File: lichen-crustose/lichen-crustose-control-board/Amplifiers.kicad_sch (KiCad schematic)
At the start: 21 parts

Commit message: Updates Lichen symbols and footprints. Fixes to Crustose and Vactrol VCA. Adds 3D model of the RP2350 dual USB board.
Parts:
- R10, R13, R14: value 4.7k_0603 -> 5.1k_0603; JLCPCB ID C23162 -> (none); Specifications 4k7, 1%, 1/10W, 0603 -> 5.1K, 1%, 1/10W, 0603
- R11, R12, R35, R36, R37, R38, R39, R40: value 100k_0603 -> 10k_0603
- R9: JLCPCB ID C23186 -> (none)
- RV1, RV2: symbol Lichen:Potentiometer -> Lichen:R_Potentiometer; now left out of the parts list
- RV10, RV3, RV4: symbol Device:R_Potentiometer_Dual -> Lichen:R_Potentiometer_Dual; now left out of the parts list
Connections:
- net CARRER_AMPLIFICATION_R: now also RV4.2; no longer RV4.5
- net CARRIER_AMPLIFICATION_L: now also RV4.5; no longer RV4.2
- net CARRIER_L: now also RV4.6; no longer RV4.1
- net CARRIER_R: now also RV4.3; no longer RV4.4
- net CARRIER_UNAMPLIFIED_L: now also RV4.1, RV4.4; no longer RV4.3, RV4.6
- net FB_L: now also RV10.6; no longer RV10.1
- net FB_R: now also RV10.3; no longer RV10.4
- net FEEDBACK_MIX_L: now also RV10.5; no longer RV10.2
- net FEEDBACK_MIX_R: now also RV10.2; no longer RV10.5
- net GND: now also RV10.1, RV10.4; no longer RV10.3, RV10.6
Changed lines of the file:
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@@
 			)
 		)
-		(property "JLCPCB ID" " C23186"
-			(at 81.28 71.12 0)
-			(effects
-				(font
-					(size 1.27 1.27)
-				)
-				(hide yes)
-			)
-		)
 		(property "LCSC" "C23186"
 			(at 98.298 74.168 0)
@@
 			)
 		)
-		(property "Value" "100k_0603"
+		(property "Value" "10k_0603"
 			(at 198.12 90.17 90)
 			(effects
@@
 			)
 		)
-		(property "Datasheet" "https://www.lcsc.com/datasheet/lcsc_datasheet_2206010045_UNI-ROYAL-Uniroyal-Elec-0603WAF1003T5E_C25803.pdf"
+		(property "Datasheet" "https://jlcpcb.com/api/file/downloadByFileSystemAccessId/8579706381320323072"
 			(at 198.12 92.71 0)
 			(effects
@@
 	)
 	(symbol
-		(lib_id "Device:R_Potentiometer_Dual")
+		(lib_id "Lichen:R_Potentiometer_Dual")
 		(at 100.33 68.58 0)
 		(unit 1)
 		(exclude_from_sim no)
-		(in_bom yes)
+		(in_bom no)
 		(on_board yes)
 		(dnp no)
@@
 		)
 		(property "Footprint" "Lichen:Potentiometer_Alpha_RD902F-40-00D_Dual_Vertical"
-			(at 106.68 70.485 0)
+			(at 107.188 80.518 0)
 			(effects
 				(font
@@
 		)
 		(property "Datasheet" "https://www.thonk.co.uk/shop/alpha-9mm-pots-vert-t18-dual-gang/"
-			(at 106.68 70.485 0)
+			(at 106.934 77.724 0)
 			(effects
 				(font
@@
 		)
 		(property "Description" "Dual potentiometer"
-			(at 100.33 68.58 0)
+			(at 100.076 83.312 0)
 			(effects
 				(font
@@
 		)
 		(property "Manufacturer" "Alpha"
-			(at 100.33 68.58 90)
+			(at 100.33 85.852 0)
 			(effects
 				(font
@@
 		)
 		(property "Part Number" "RD90F-40"
-			(at 100.33 68.58 90)
+			(at 100.33 88.138 0)
 			(effects
 				(font
@@
 			)
 		)
-		(property "Value" "4.7k_0603"
+		(property "Value" "5.1k_0603"
 			(at 83.82 129.54 90)
 			(effects
@@
 			)
 		)
-		(property "Specifications" "4k7, 1%, 1/10W, 0603"
+		(property "Specifications" "5.1K, 1%, 1/10W, 0603"
 			(at 91.694 129.54 0)
 			(effects
@@
 			)
 		)
-		(property "JLCPCB ID" "C23162"
-			(at 83.82 132.08 0)
-			(effects
-				(font
-					(size 1.27 1.27)
-				)
-				(hide yes)
-			)
-		)
 		(property "LCSC" "C23186"
 			(at 100.838 135.128 0)
@@
 	)
 	(symbol
-		(lib_id "Lichen:Potentiometer")
+		(lib_id "Lichen:R_Potentiometer")
 		(at 71.12 149.86 0)
 		(mirror x)
 		(unit 1)
 		(exclude_from_sim no)
-		(in_bom yes)
+		(in_bom no)
 		(on_board yes)
 		(dnp no)
 		(fields_autoplaced yes)
 		(property "Reference" "RV1"
-			(at 68.58 151.1301 0)
+			(at 67.31 148.5899 0)
 			(effects
 				(font
@@
 		)
 		(property "Value" "B10K"
-			(at 68.58 148.5901 0)
+			(at 67.31 151.1299 0)
 			(effects
 				(font
@@
 			)
 		)
-		(property "Value" "100k_0603"
+		(property "Value" "10k_0603"
 			(at 198.12 72.39 90)
 			(effects
@@
 			)
 		)
-		(property "Datasheet" "https://www.lcsc.com/datasheet/lcsc_datasheet_2206010045_UNI-ROYAL-Uniroyal-Elec-0603WAF1003T5E_C25803.pdf"
+		(property "Datasheet" "https://jlcpcb.com/api/file/downloadByFileSystemAccessId/8579706381320323072"
 			(at 198.12 74.93 0)
 			(effects
@@
 			)
 		)
-		(property "Value" "100k_0603"
+		(property "Value" "10k_0603"
 			(at 83.82 147.32 90)
 			(effects
@@
 			)
 		)
-		(property "Datasheet" "https://www.lcsc.com/datasheet/lcsc_datasheet_2206010045_UNI-ROYAL-Uniroyal-Elec-0603WAF1003T5E_C25803.pdf"
+		(property "Datasheet" "https://jlcpcb.com/api/file/downloadByFileSystemAccessId/8579706381320323072"
 			(at 83.82 149.86 0)
 			(effects
@@
 			)
 		)
-		(property "Datasheet" ""
+		(property "Datasheet" "https://jlcpcb.com/api/file/downloadByFileSystemAccessId/8579707056569573376"
 			(at 217.17 72.39 0)
 			(effects
@@
 			)
 		)
-		(property "Value" "4.7k_0603"
+		(property "Value" "5.1k_0603"
 			(at 83.82 119.38 90)
 			(effects
@@
 			)
 		)
-		(property "Specifications" "4k7, 1%, 1/10W, 0603"
+		(property "Specifications" "5.1K, 1%, 1/10W, 0603"
 			(at 91.694 119.38 0)
 			(effects
@@
 			)
 		)
-		(property "JLCPCB ID" "C23162"
-			(at 83.82 121.92 0)
-			(effects
-				(font
-					(size 1.27 1.27)
-				)
-				(hide yes)
-			)
-		)
 		(property "LCSC" "C23186"
 			(at 100.838 124.968 0)
@@
 			)
 		)
-		(property "Value" "100k_0603"
+		(property "Value" "10k_0603"
 			(at 198.12 43.18 90)
 			(effects
@@
 			)
 		)
-		(property "Datasheet" "https://www.lcsc.com/datasheet/lcsc_datasheet_2206010045_UNI-ROYAL-Uniroyal-Elec-0603WAF1003T5E_C25803.pdf"
+		(property "Datasheet" "https://jlcpcb.com/api/file/downloadByFileSystemAccessId/8579706381320323072"
 			(at 198.12 45.72 0)
 			(effects
@@
 			)
 		)
-		(property "Value" "100k_0603"
+		(property "Value" "10k_0603"
 			(at 83.82 173.99 90)
 			(effects
@@
 			)
 		)
-		(property "Datasheet" "https://www.lcsc.com/datasheet/lcsc_datasheet_2206010045_UNI-ROYAL-Uniroyal-Elec-0603WAF1003T5E_C25803.pdf"
+		(property "Datasheet" "https://jlcpcb.com/api/file/downloadByFileSystemAccessId/8579706381320323072"
 			(at 83.82 176.53 0)
 			(effects
@@
 			)
 		)
-		(property "Value" "4.7k_0603"
+		(property "Value" "5.1k_0603"
 			(at 81.28 80.01 90)
 			(effects
@@
 			)
 		)
-		(property "Specifications" "4k7, 1%, 1/10W, 0603"
+		(property "Specifications" "5.1K, 1%, 1/10W, 0603"
 			(at 89.154 80.01 0)
 			(effects
@@
 			)
 		)
-		(property "JLCPCB ID" "C23162"
-			(at 81.28 82.55 0)
-			(effects
-				(font
-					(size 1.27 1.27)
-				)
-				(hide yes)
-			)
-		)
 		(property "LCSC" "C23186"
 			(at 98.298 85.598 0)
@@
 			)
 		)
-		(property "Value" "100k_0603"
+		(property "Value" "10k_0603"
 			(at 215.9 39.37 90)
 			(effects
@@
 			)
 		)
-		(property "Datasheet" "https://www.lcsc.com/datasheet/lcsc_datasheet_2206010045_UNI-ROYAL-Uniroyal-Elec-0603WAF1003T5E_C25803.pdf"
+		(property "Datasheet" "https://jlcpcb.com/api/file/downloadByFileSystemAccessId/8579706381320323072"
 			(at 215.9 36.83 0)
 			(effects
@@
 			)
 		)
-		(property "Value" "100k_0603"
+		(property "Value" "10k_0603"
 			(at 217.17 86.36 90)
 			(effects
@@
 			)
 		)
-		(property "Datasheet" "https://www.lcsc.com/datasheet/lcsc_datasheet_2206010045_UNI-ROYAL-Uniroyal-Elec-0603WAF1003T5E_C25803.pdf"
+		(property "Datasheet" "https://jlcpcb.com/api/file/downloadByFileSystemAccessId/8579706381320323072"
 			(at 217.17 83.82 0)
 			(effects
@@
 	)
 	(symbol
-		(lib_id "Device:R_Potentiometer_Dual")
+		(lib_id "Lichen:R_Potentiometer_Dual")
 		(at 189.23 68.58 270)
+		(mirror x)
 		(unit 1)
 		(exclude_from_sim no)
-		(in_bom yes)
+		(in_bom no)
 		(on_board yes)
 		(dnp no)
 		(property "Reference" "RV10"
-			(at 183.134 61.976 0)
+			(at 183.134 75.184 0)
 			(effects
 				(font
@@
 		)
 		(property "Value" "B10k_Dual"
-			(at 183.134 75.438 0)
+			(at 183.134 61.722 0)
 			(effects
 				(font
@@
 		)
 		(property "Footprint" "Lichen:Potentiometer_Alpha_RD902F-40-00D_Dual_Vertical"
-			(at 187.325 74.93 0)
+			(at 177.292 61.722 0)
 			(effects
 				(font
@@
 		)
 		(property "Datasheet" "https://www.thonk.co.uk/shop/alpha-9mm-pots-vert-t18-dual-gang/"
-			(at 187.325 74.93 0)
+			(at 180.086 61.976 0)
 			(effects
 				(font
@@
 		)
 		(property "Description" "Dual potentiometer"
-			(at 189.23 68.58 0)
+			(at 174.498 68.834 0)
 			(effects
 				(font
@@
 		)
 		(property "Manufacturer" "Alpha"
-			(at 189.23 68.58 90)
+			(at 171.958 68.58 0)
 			(effects
 				(font
@@
 		)
 		(property "Part Number" "RD90F-40"
-			(at 189.23 68.58 90)
+			(at 169.672 68.58 0)
 			(effects
 				(font
@@
 	)
 	(symbol
-		(lib_id "Device:R_Potentiometer_Dual")
-		(at 121.92 143.51 180)
+		(lib_id "Lichen:R_Potentiometer_Dual")
+		(at 121.92 143.51 0)
+		(mirror x)
 		(unit 1)
 		(exclude_from_sim no)
-		(in_bom yes)
+		(in_bom no)
 		(on_board yes)
 		(dnp no)
 		(property "Reference" "RV4"
-			(at 128.524 137.414 0)
+			(at 115.316 137.414 0)
 			(effects
 				(font
@@
 		)
 		(property "Value" "A10k_Dual"
-			(at 115.062 137.414 0)
+			(at 128.778 137.414 0)
 			(effects
 				(font
@@
 		)
 		(property "Footprint" "Lichen:Potentiometer_Alpha_RD902F-40-00D_Dual_Vertical"
-			(at 115.57 141.605 0)
+			(at 128.778 131.572 0)
 			(effects
 				(font
@@
 		)
 		(property "Datasheet" "https://www.thonk.co.uk/shop/alpha-9mm-pots-vert-t18-dual-gang/"
-			(at 115.57 141.605 0)
+			(at 128.524 134.366 0)
 			(effects
 				(font
@@
 		)
 		(property "Description" "Dual potentiometer"
-			(at 121.92 143.51 0)
+			(at 121.666 128.778 0)
 			(effects
 				(font
@@
 		)
 		(property "Manufacturer" "Alpha"
-			(at 121.92 143.51 90)
+			(at 121.92 126.238 0)
 			(effects
 				(font
@@
 		)
 		(property "Part Number" "RD90F-40"
-			(at 121.92 143.51 90)
+			(at 121.92 123.952 0)
 			(effects
 				(font
@@
 	)
 	(symbol
-		(lib_id "Lichen:Potentiometer")
+		(lib_id "Lichen:R_Potentiometer")
 		(at 71.12 176.53 0)
 		(mirror x)
 		(unit 1)
 		(exclude_from_sim no)
-		(in_bom yes)
+		(in_bom no)
 		(on_board yes)
 		(dnp no)
@@
 			)
 		)
-		(property "Value" "100k_0603"
+		(property "Value" "10k_0603"
 			(at 198.12 59.69 90)
 			(effects
@@
 			)
 		)
-		(property "Datasheet" "https://www.lcsc.com/datasheet/lcsc_datasheet_2206010045_UNI-ROYAL-Uniroyal-Elec-0603WAF1003T5E_C25803.pdf"
+		(property "Datasheet" "https://jlcpcb.com/api/file/downloadByFileSystemAccessId/8579706381320323072"
 			(at 198.12 62.23 0)
 			(effects

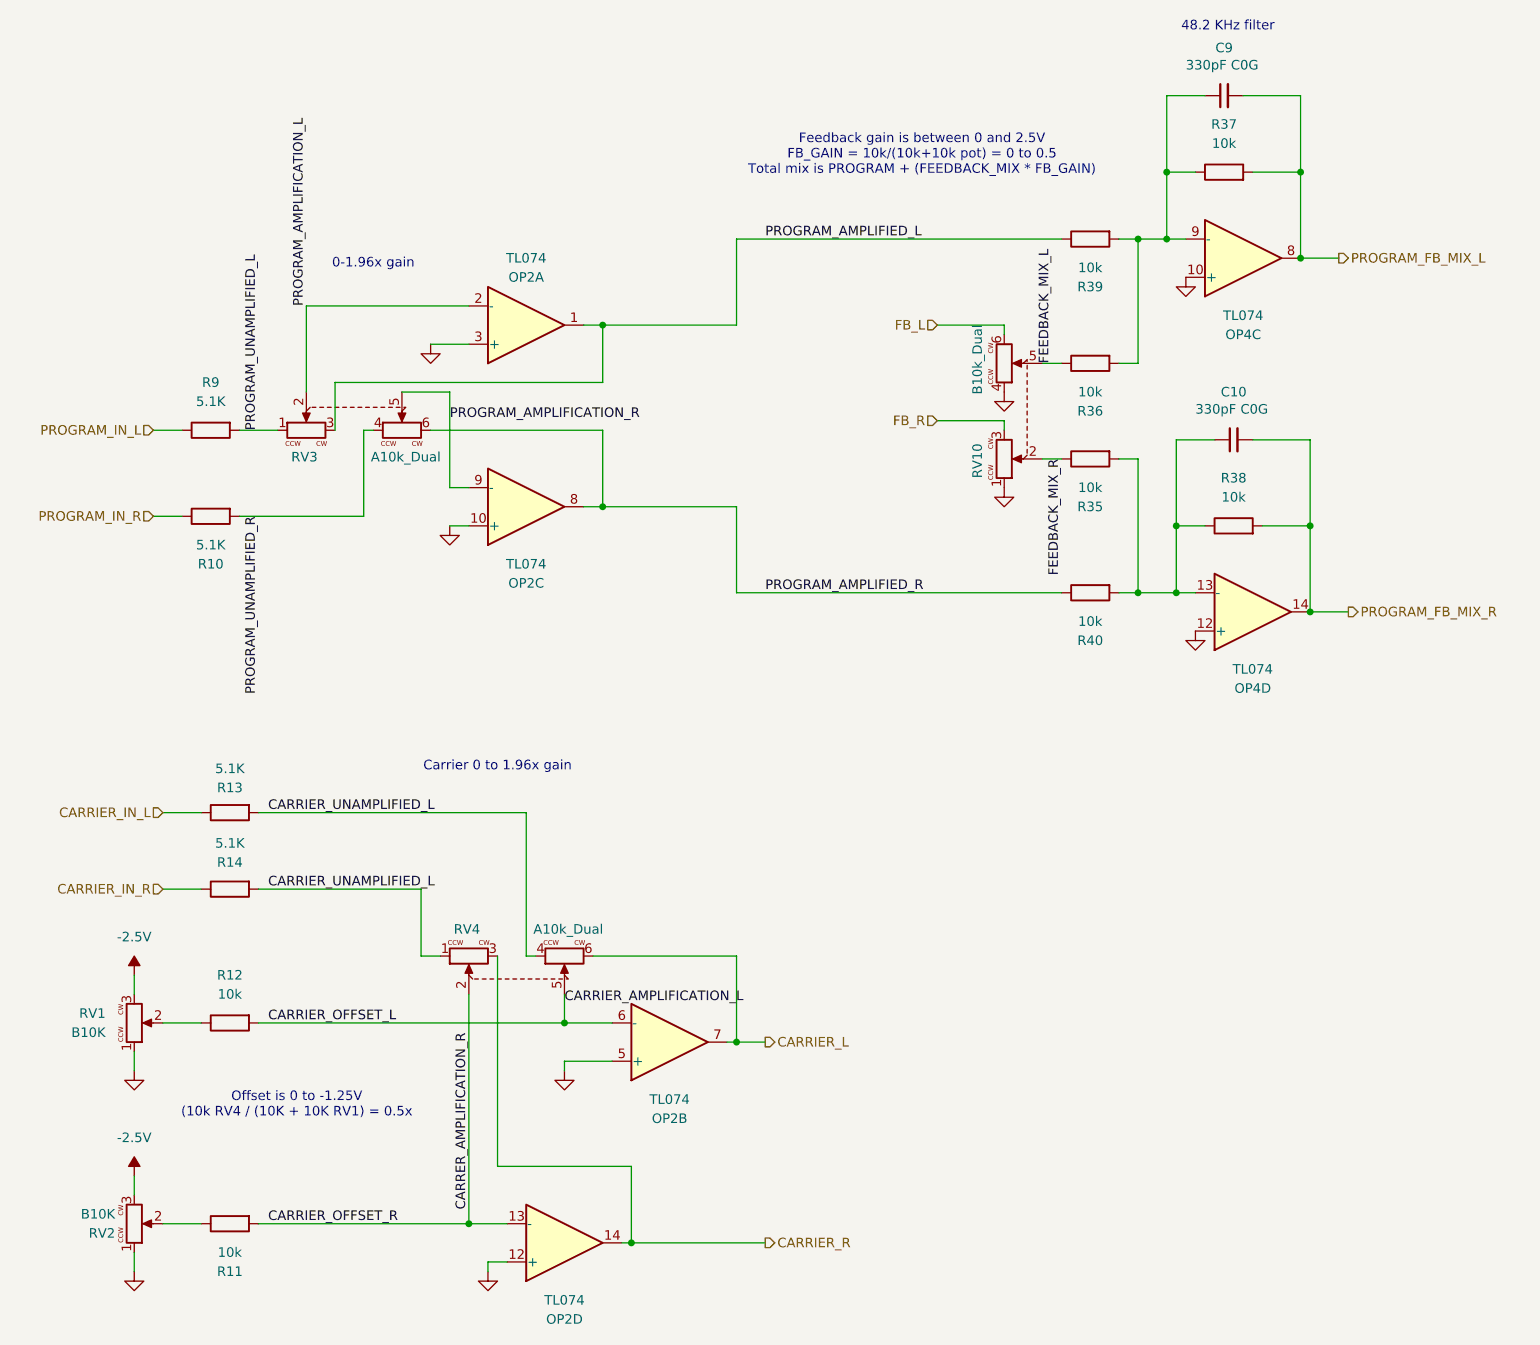
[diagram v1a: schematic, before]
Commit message: feat: Updates Crustose, Cladonia and YouMe Transformer. Adds Stereo Latencies.
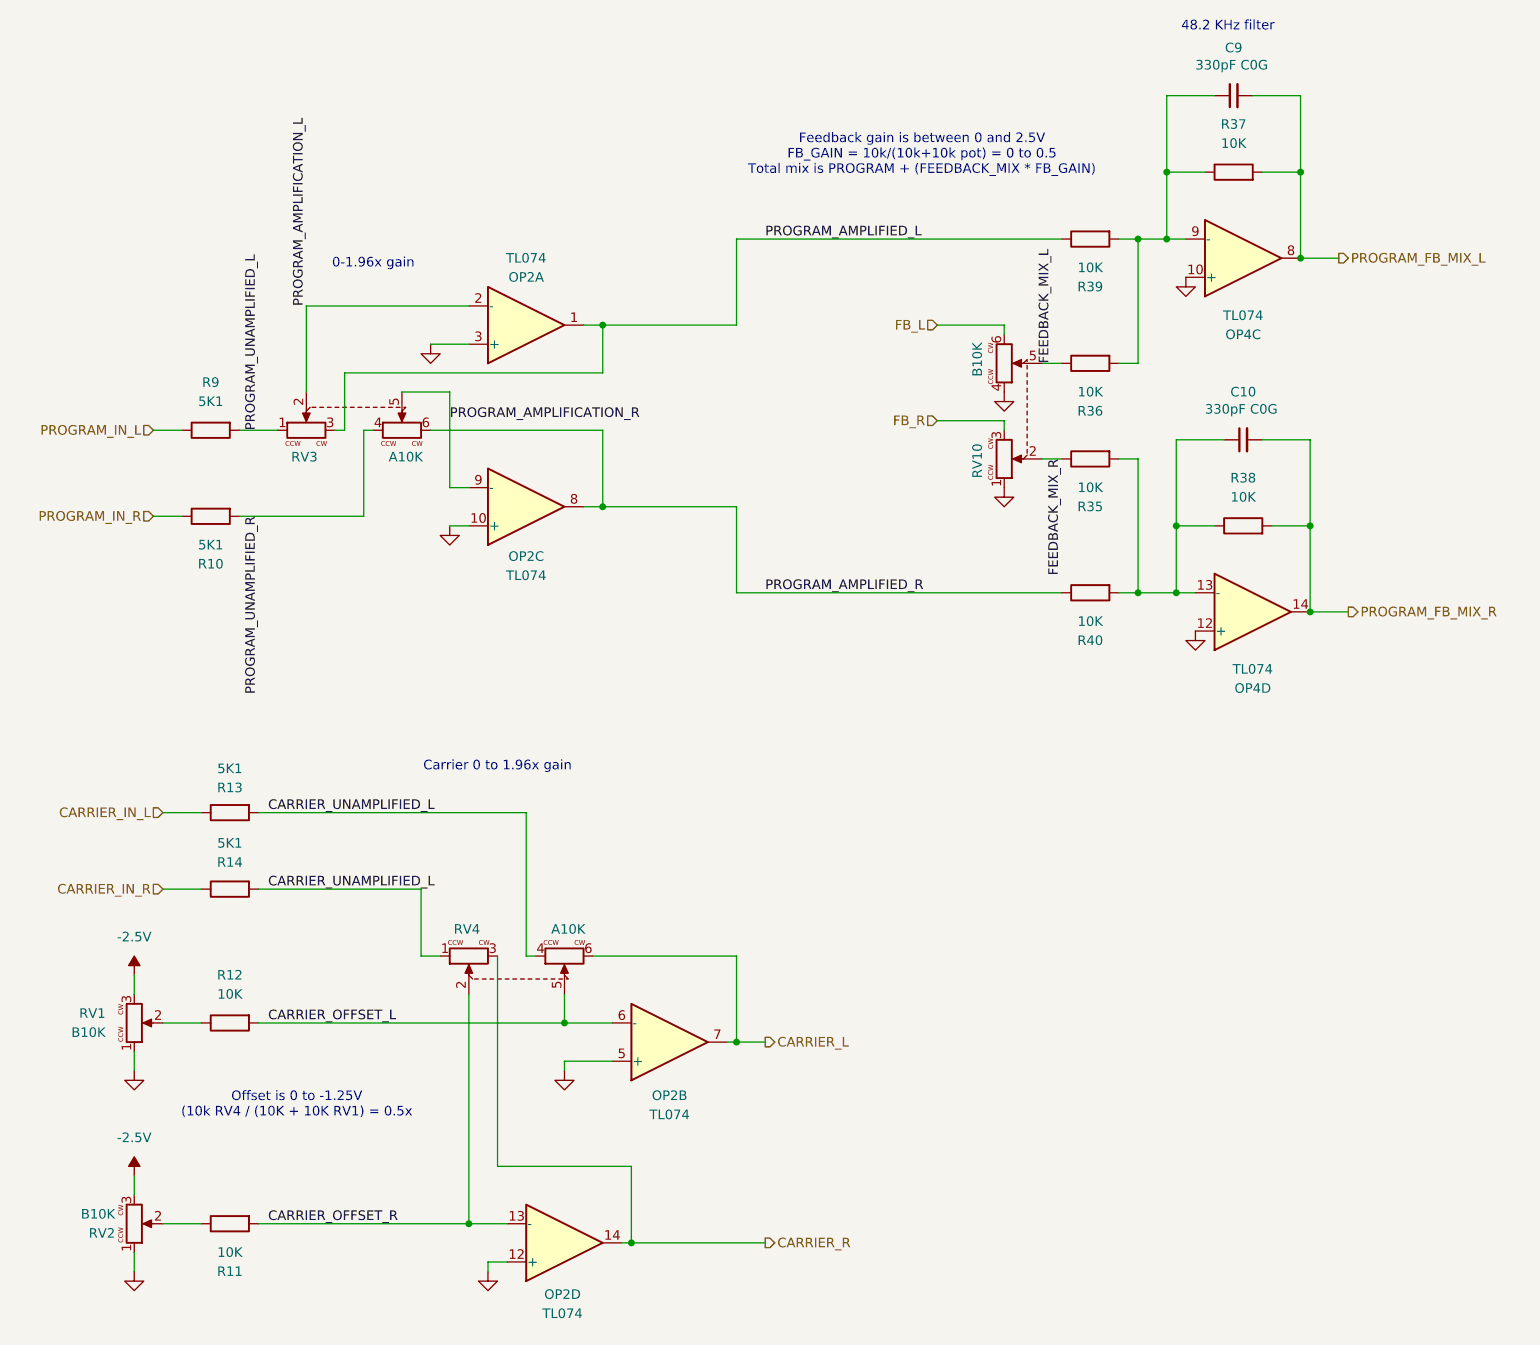
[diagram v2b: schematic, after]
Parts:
- OP2: symbol Amplifier_Operational:TL074 -> Lichen:TL074; LCSC C6963 -> C6964; Manufacturer STMicroelectronics -> Texas Instruments; Part Number TL074CDT -> TL074IDR
- OP4: symbol Amplifier_Operational:TL074 -> Lichen:TL074; LCSC (none) -> C6964; Manufacturer (none) -> Texas Instruments; Part Number (none) -> TL074IDR
- R10, R13, R14: value 5.1k_0603 -> 5.1K; Display 5.1K -> 5K1; Specifications 5.1K, 1%, 1/10W, 0603 -> (none)
- R11, R12, R35, R36, R37, R38, R39, R40: value 10k_0603 -> 10K; Display 10k -> 10K; JLCPCB ID C25804 -> (none); LCSC (none) -> C25804
- R9: value 5.1k_0603 -> 5.1K; Display 5.1K -> 5K1; Specifications 5k1, 1%, 1/10W, 0603 -> (none)
- RV10: value B10k_Dual -> B10K
- RV3, RV4: value A10k_Dual -> A10K
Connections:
- net CARRER_AMPLIFICATION_R renamed CARRIER_OFFSET_R
- net CARRIER_AMPLIFICATION_L renamed CARRIER_OFFSET_L
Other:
- moved on the sheet: C10, C9, R37, R38
